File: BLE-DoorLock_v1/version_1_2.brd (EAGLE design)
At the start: 54.6 x 100 mm, 33 parts, among them K1 G5LE-14_DC12, Q1 MMBT2222, Q2 MMBT2222, Q3 DMN6140L

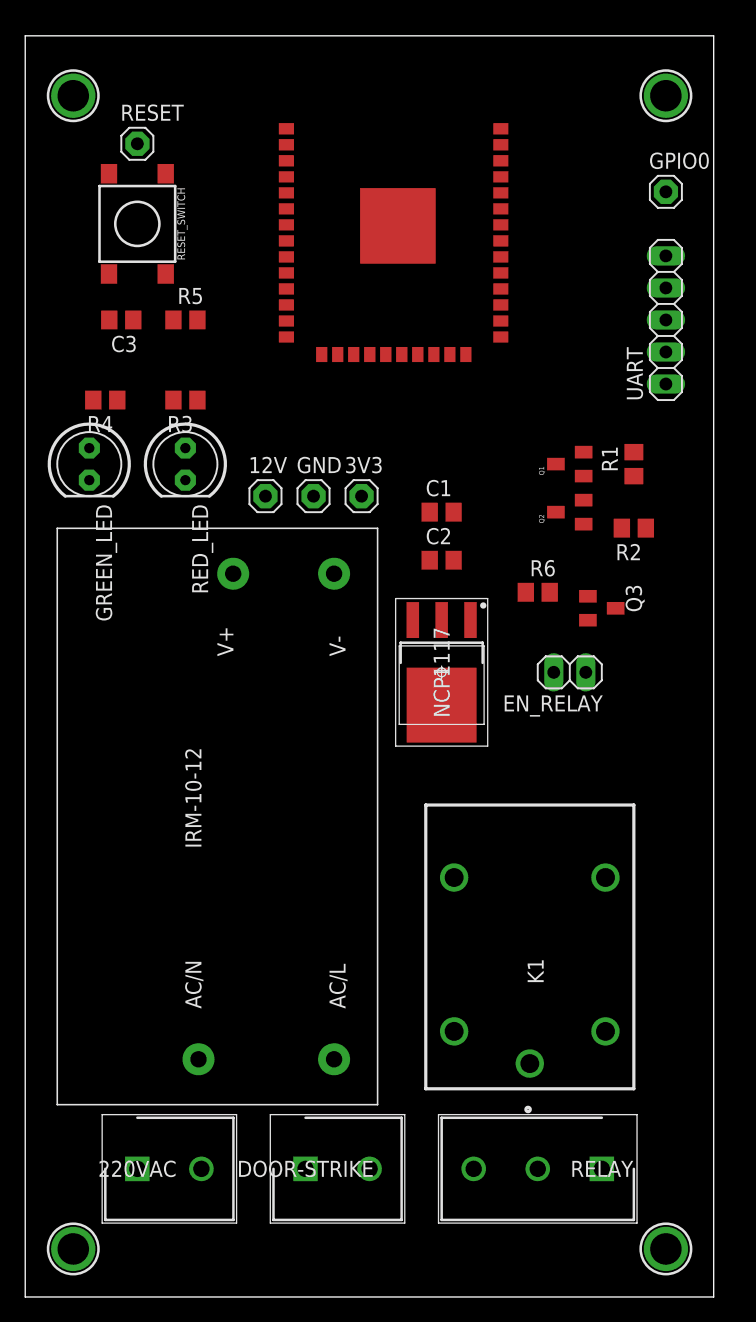
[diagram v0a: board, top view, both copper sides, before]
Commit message: Demo PCB -with relay- version_1.2
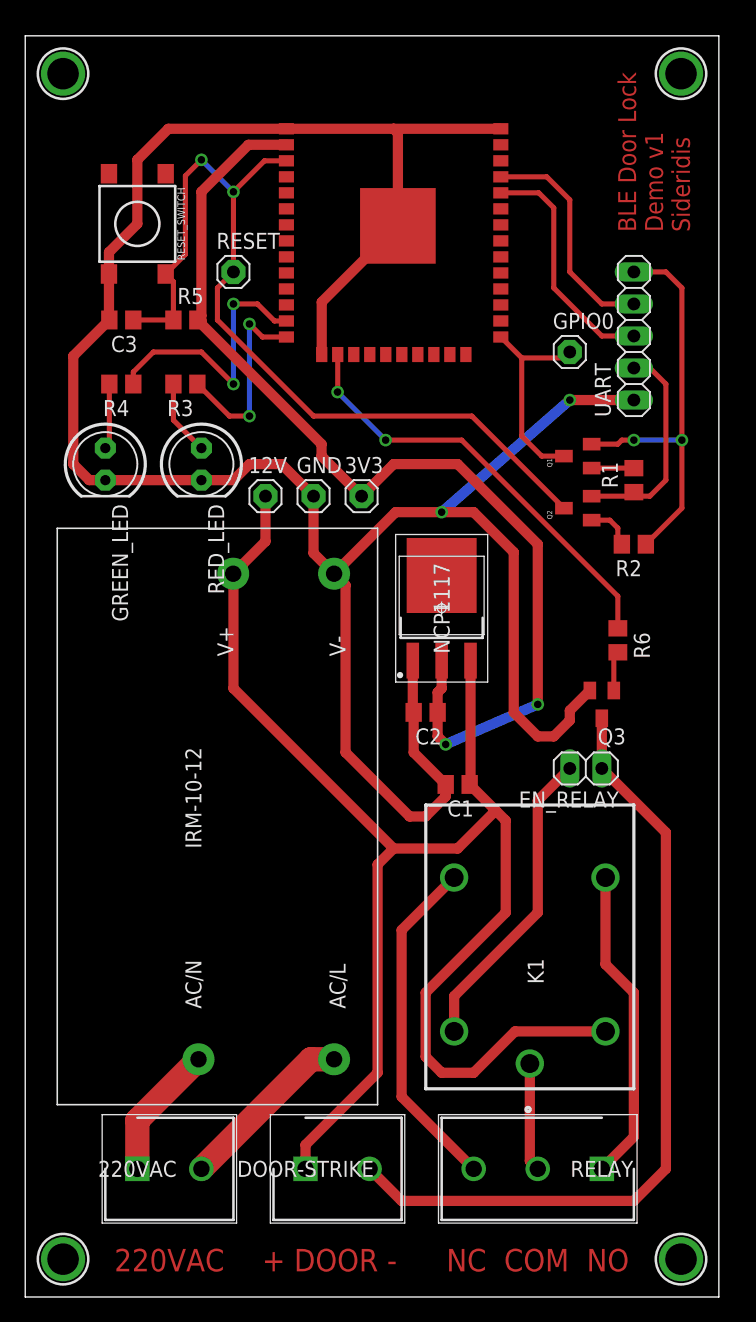
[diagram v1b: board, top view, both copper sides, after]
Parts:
- moved C1 21.6 mm to (34.3, 40.6), turned to 180 degrees
- moved GPIO0 14.8 mm to (43.2, 74.9)
- moved RESET 12.7 mm to (16.5, 81.3)
- moved C2 12.1 mm to (31.8, 46.4), turned to 180 degrees
- moved EN_RELAY 7.73 mm to (44.5, 41.9)
- moved Q3 7.62 mm to (45.7, 47.0), turned to 180 degrees
- moved R6 7.41 mm to (47.0, 52.1), turned to 270 degrees
- moved NCP1117 5.08 mm to (33.0, 54.6), turned to 90 degrees
- moved UART 2.84 mm to (48.3, 76.2)
- moved U$1 2.12 mm to (52.0, 97.0)
- moved U$4 1.93 mm to (3.00, 97.0)
- moved R4 1.80 mm to (7.62, 72.4)
- moved U$3 1.45 mm to (52.0, 3.00)
- moved R1 1.27 mm to (48.3, 64.8)
- moved R2 1.27 mm to (48.3, 59.7)
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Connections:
- net RXD0: now also UART.3; no longer UART.4
- net TXD0: now also UART.4; no longer UART.3
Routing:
- net GND: track 0.00 -> 199.4 mm, vias 0 -> 2
- net +12V: track 0.00 -> 123.3 mm
- net +3V3: track 0.00 -> 83.5 mm, vias 0 -> 2
- net RESET: track 0.00 -> 70.5 mm, vias 0 -> 2
- net LOCK_N: track 0.00 -> 63.4 mm
- net GPIO13: track 0.00 -> 34.5 mm, vias 0 -> 2
- net DTR: track 0.00 -> 33.1 mm, vias 0 -> 2
- net NC: track 0.00 -> 27.2 mm
- net NO: track 0.00 -> 25.1 mm
- net N$8: track 0.00 -> 24.6 mm
- net GPIO14: track 0.00 -> 21.7 mm, vias 0 -> 2
- net RXD0: track 0.00 -> 19.0 mm
- net TXD0: track 0.00 -> 18.1 mm
- net RTS: track 0.00 -> 17.4 mm
- net GPIO0: track 0.00 -> 16.6 mm
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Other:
- board size 54.6 x 100 mm -> 55 x 100 mm
- board text added: "+ DOOR -"
- board text added: "220VAC"
- board text added: "BLE Door Lock Demo v1 Sideridis"
- board text added: "NC COM NO"
